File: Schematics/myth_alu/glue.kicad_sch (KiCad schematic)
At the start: 5 parts, among them U15 74LS32, U18 4075, U4 74HC04, U6 74LS21, U7 74LS08

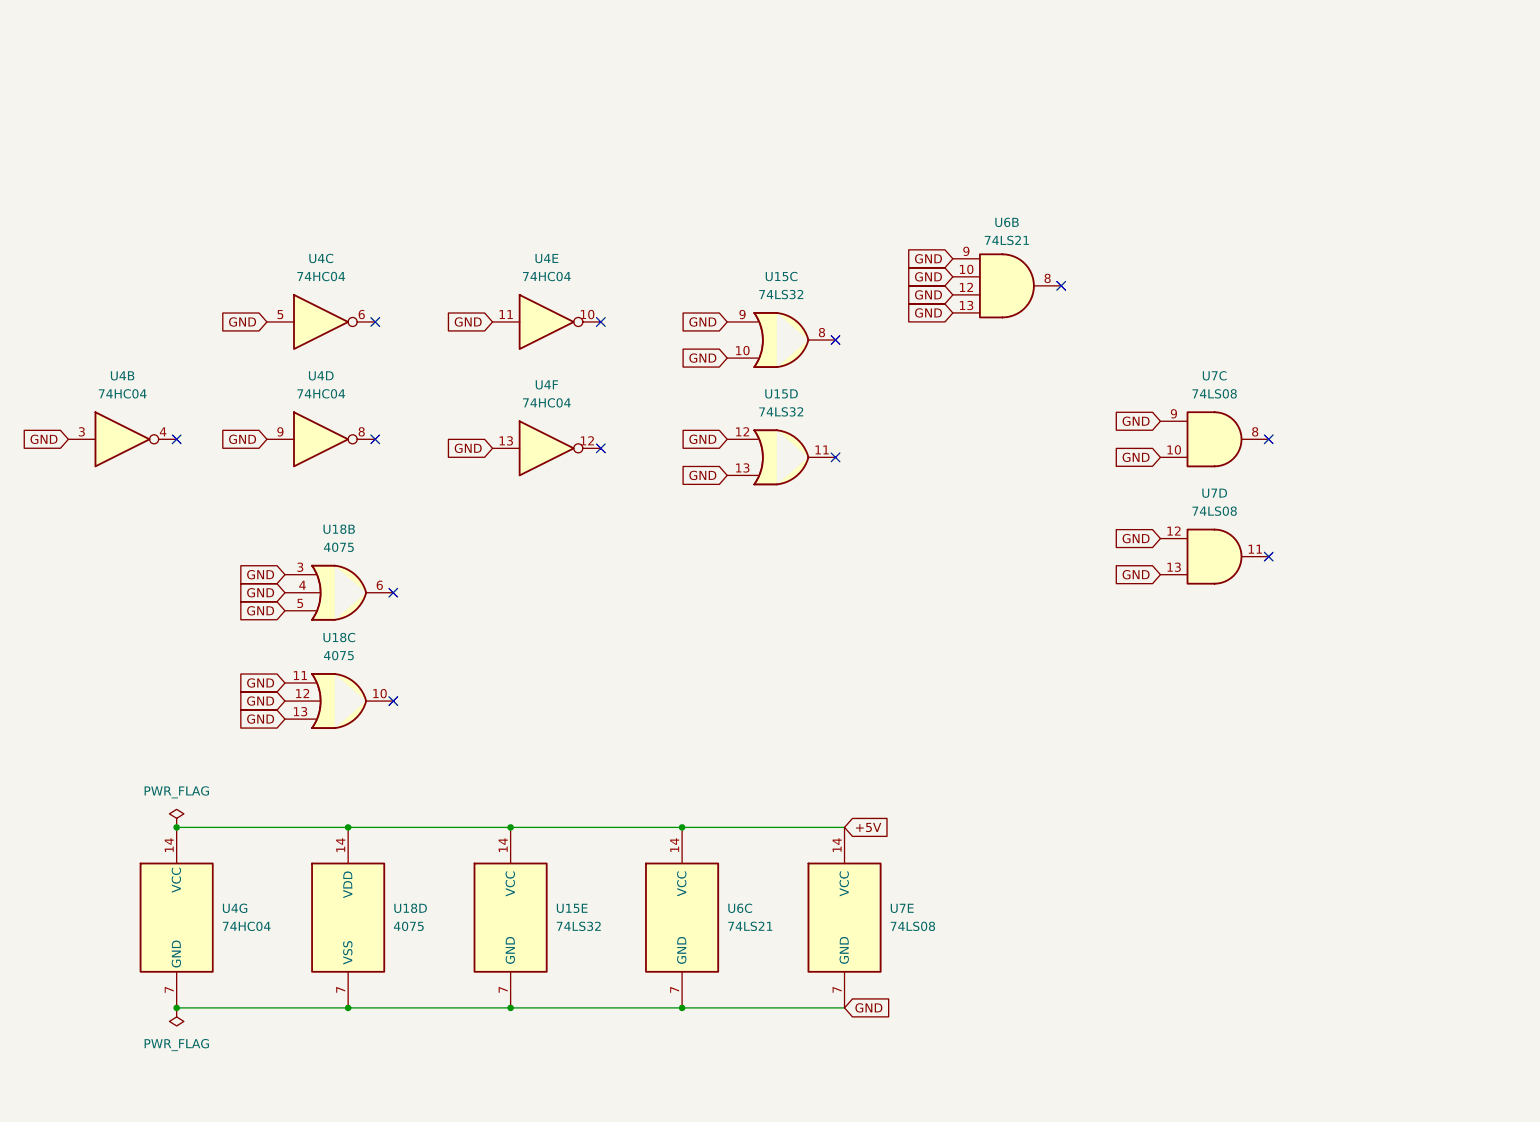
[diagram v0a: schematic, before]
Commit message: Change d to g
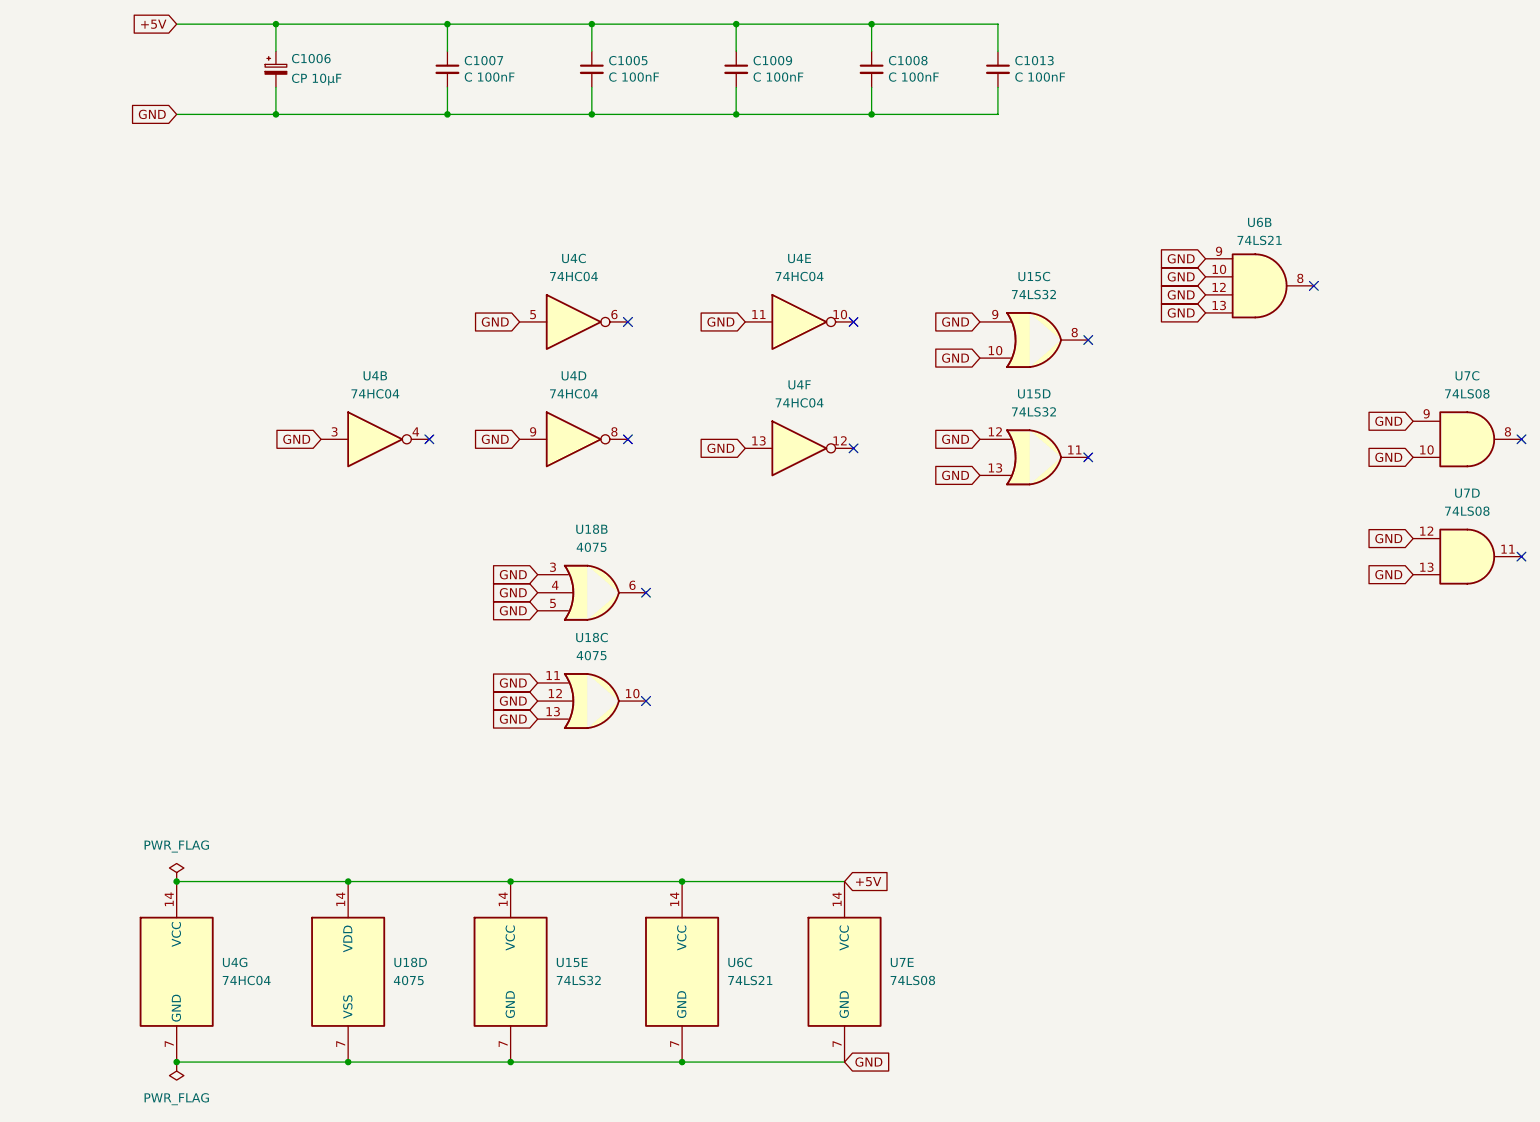
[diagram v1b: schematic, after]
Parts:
- added C1005, C1007, C1008, C1009, C1013: C 100nF, Capacitor_THT:C_Disc_D5.0mm_W2.5mm_P2.50mm, symbol Device:C_Small
- added C1006: CP 10μF, Capacitor_THT:CP_Radial_D6.3mm_P2.50mm, symbol Device:C_Polarized_Small
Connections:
- net +5V: now also C1005.1, C1006.1, C1007.1, C1008.1, C1009.1, C1013.1
- net GND: now also C1005.2, C1006.2, C1007.2, C1008.2, C1009.2, C1013.2
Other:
- moved on the sheet: U15C, U15D, U15E, U18B, U18C, U18D, U4B, U4C, U4D, U4E, U4F, U4G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

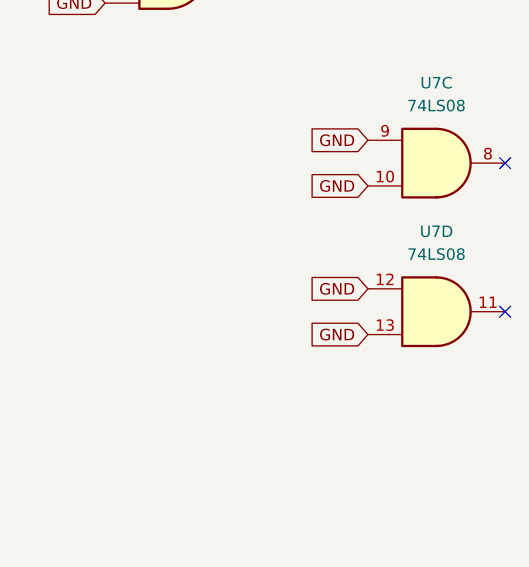
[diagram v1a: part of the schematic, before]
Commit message: Change COR to use R
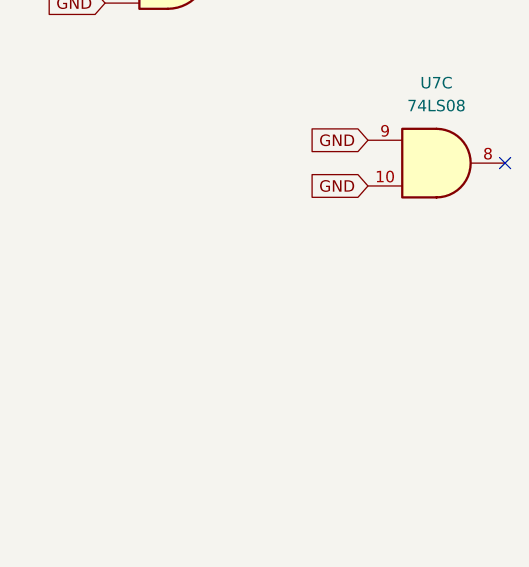
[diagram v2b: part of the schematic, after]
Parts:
- removed unit 4 of U7
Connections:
- no-connect marks 12 -> 11
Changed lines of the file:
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@@
-	)
-	(no_connect
-		(at 236.22 101.6)
 	)
 	(no_connect
@@
 	(global_label "GND"
 		(shape input)
-		(at 220.98 104.14 180)
-		(fields_autoplaced yes)
-		(effects
-			(font
-				(size 1.27 1.27)
-			)
-			(justify right)
-		)
-		(property "Intersheetrefs" "${INTERSHEET_REFS}"
-			(at 214.1243 104.14 0)
-			(effects
-				(font
-					(size 1.27 1.27)
-				)
-				(justify right)
-				(hide yes)
-			)
-		)
-	)
-	(global_label "GND"
-		(shape input)
 		(at 160.02 90.17 180)
 		(fields_autoplaced yes)
@@
 		(property "Intersheetrefs" "${INTERSHEET_REFS}"
 			(at 88.3943 85.09 0)
-			(effects
-				(font
-					(size 1.27 1.27)
-				)
-				(justify right)
-				(hide yes)
-			)
-		)
-	)
-	(global_label "GND"
-		(shape input)
-		(at 220.98 99.06 180)
-		(fields_autoplaced yes)
-		(effects
-			(font
-				(size 1.27 1.27)
-			)
-			(justify right)
-		)
-		(property "Intersheetrefs" "${INTERSHEET_REFS}"
-			(at 214.1243 99.06 0)
 			(effects
 				(font
@@
 				)
 			)
-		)
-	)
-	(symbol
-		(lib_id "74xx:74LS08")
-		(at 228.6 101.6 0)
-		(unit 4)
-		(exclude_from_sim no)
-		(in_bom yes)
-		(on_board yes)
-		(dnp no)
-		(fields_autoplaced yes)
-		(property "Reference" "U7"
-			(at 228.5917 92.71 0)
-			(effects
-				(font
-					(size 1.27 1.27)
-				)
-			)
-		)
-		(property "Value" "74LS08"
-			(at 228.5917 95.25 0)
-			(effects
-				(font
-					(size 1.27 1.27)
-				)
-			)
-		)
-		(property "Footprint" "Package_DIP:DIP-14_W7.62mm_Socket_LongPads"
-			(at 228.6 101.6 0)
-			(effects
-				(font
-					(size 1.27 1.27)
-				)
-				(hide yes)
-			)
-		)
-		(property "Datasheet" "http://www.ti.com/lit/gpn/sn74LS08"
-			(at 228.6 101.6 0)
-			(effects
-				(font
-					(size 1.27 1.27)
-				)
-				(hide yes)
-			)
-		)
-		(property "Description" "Quad And2"
-			(at 228.6 101.6 0)
-			(effects
-				(font
-					(size 1.27 1.27)
-				)
-				(hide yes)
-			)
-		)
-		(pin "1"
-		)
-		(pin "2"
-		)
-		(pin "3"
-		)
-		(pin "4"
-		)
-		(pin "5"
-		)
-		(pin "6"
-		)
-		(pin "10"
-		)
-		(pin "8"
-		)
-		(pin "9"
-		)
-		(pin "11"
-		)
-		(pin "12"
-		)
-		(pin "13"
-		)
-		(pin "14"
-		)
-		(pin "7"
-		)
-		(instances
-			(project "myth_alu"
-				(path "/dc50927e-cadd-41f6-9ed1-9781b4a3fe94/fccc726a-f35b-4dec-b550-8b01869cab59"
-					(reference "U7")
-					(unit 4)
-				)
-			)
